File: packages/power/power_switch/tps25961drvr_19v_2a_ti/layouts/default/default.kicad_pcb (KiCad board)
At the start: 2 copper layers, 6 parts

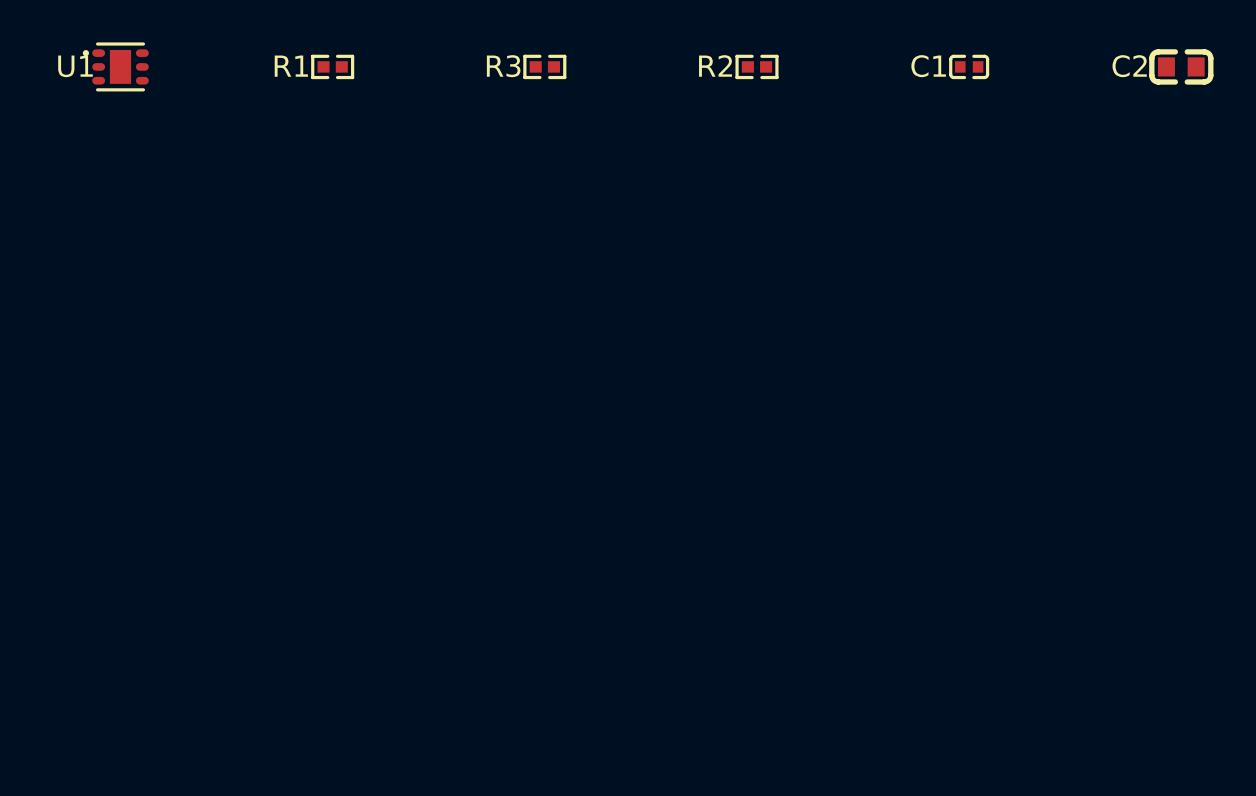
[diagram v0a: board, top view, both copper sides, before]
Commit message: TPS25961 layout
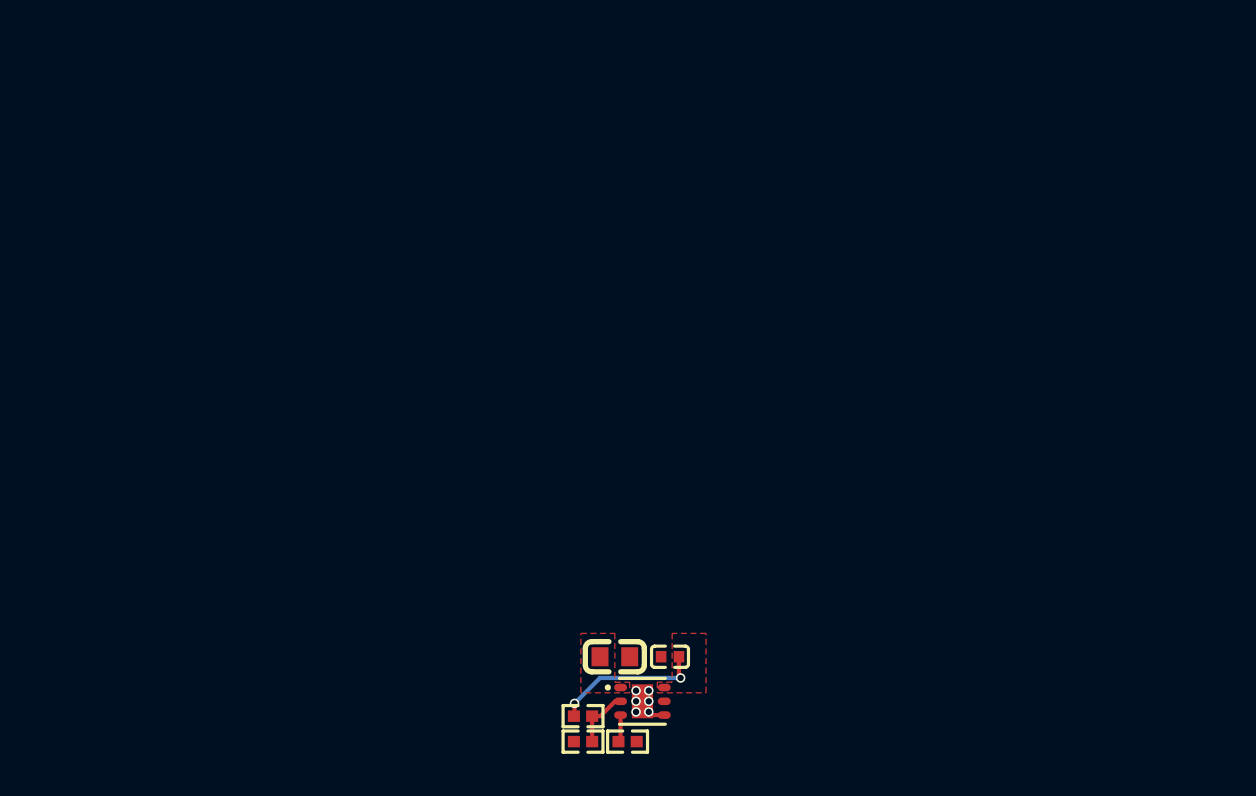
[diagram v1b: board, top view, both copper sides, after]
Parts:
- moved U1 38.7 mm to (24.6, 29.9)
- moved C2 38.5 mm to (23.3, 27.8)
- moved R1 34.7 mm to (23.9, 31.8)
- moved R2 32.8 mm to (21.8, 31.8), turned to 180 degrees
- moved C1 31.2 mm to (25.9, 27.8), turned to 180 degrees
- moved R3 30.7 mm to (21.8, 30.6)
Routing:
- net power_in-hv: track 0.00 -> 7.14 mm, vias 0 -> 2
- net 2: track 0.00 -> 2.83 mm
- net ILIM: track 0.00 -> 1.29 mm
- net lv: track 0.00 -> 1.09 mm, vias 0 -> 6
- added copper zone on F.Cu, net hv
- added copper zone on F.Cu, net power_in-hv
